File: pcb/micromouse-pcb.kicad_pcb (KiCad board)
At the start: 4 copper layers, 100 x 120 mm, 156 parts, among them J1 JST_PH_B2B-PH-K_1x02_P2.00mm_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, J5 JST_PH_B6B-PH-K_1x06_P2.00mm_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, J6 JST_PH_B6B-PH-K_1x06_P2.00mm_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, J7 USB_C_Receptacle_GCT_USB4105-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, J8 PinHeader_1x06_P2.54mm_Vertic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, Q1 SOT-23, Q16 SOT-23, Q17 SOT-23, Q18 SOT-23, Q19 SOT-23, Q2 LED_D5.0mm_IRBlack, Q20 SOT-23, Q21 SOT-23, Q22 SOT-23, Q23 SOT-23, Q24 SOT-23, Q25 SOT-23, Q26 SOT-23, Q27 SOT-23, Q28 SOT-23, Q29 SOT-23, Q3 LED_D5.0mm_IRBlack, Q30 SOT-23, Q31 SOT-23, Q32 SOT-23, Q33 SOT-23, Q4 LED_D5.0mm_IRBlack, Q5 LED_D5.0mm_IRBlack, Q6 LED_D5.0mm_IRBlack, Q7 LED_D5.0mm_IRBlack, SW1 SW_PUSH_6mm, SW2 SW_PUSH_6mm, SW3 SW_PUSH_6mm, SW4 SW_PUSH_6mm, SW5 SW_Slide_SPDT_Straight_CK_OS1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, U1 Texas_DRC0010J_ThermalVias, U2 SSOP-24_5.3x8.2mm_P0.65mm, U3 ESP32-S3-WROOM-1, U4 SOIC-24W_7.5x15.4mm_P1.27mm, U6 SOT-23-6

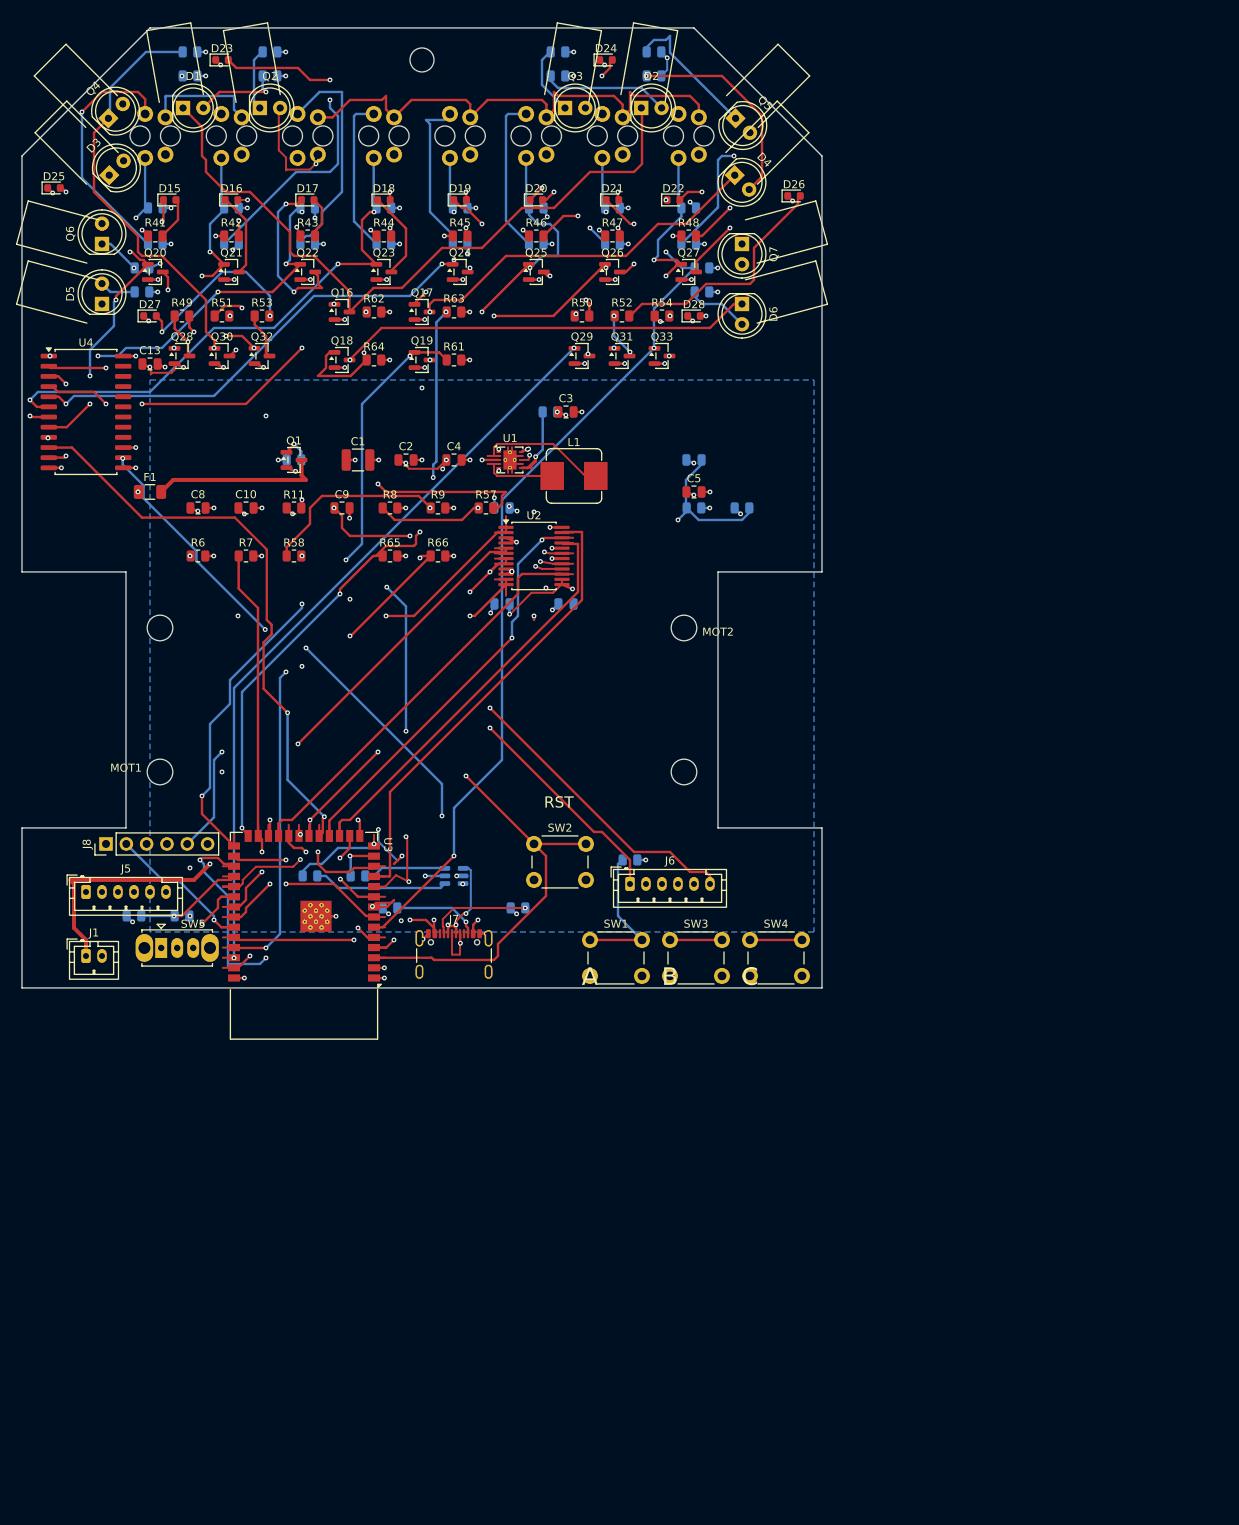
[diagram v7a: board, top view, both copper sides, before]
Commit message: Rev 6.1: 2S power, regulated 6V motors, BNO055 IMU, dual switches + full handoff
Design + firmware + verification COMPLETE and passing; PCB routed to 5
remaining unconnected edges (all in the USB-C connector fanout + the Q1 gate,
documented exactly in HANDOFF.md). This commit is a self-contained handoff so
the board can be finished on another machine with no human input.

Rev 6 (all 10 user requirements, each gated):
- 2S LiPo -> AP63203 3.3V + TPS54302 regulated 6.0V motor rail; DMP3098L
  reverse-FET (Vgs +/-20V, 2S-safe); dual switches (SW5 all / SW6 motors).
- BNO055 9-axis IMU on the centerline (I2C); external crystal DROPPED
  (internal oscillator, spec-supported) after it proved unroutable at the
  0.5mm-pitch LGA.
- Exact wall-sensor aims 0/45/90 deg with silk angle callouts; sensor
  outlines fully inside the board with a 3-5mm edge gap.
- Antenna spans a rear-edge U-notch (nothing outside the outline but shafts).
- USB-C direct D+/D-, IN/IN motor drive, per-cell battery monitoring.
- BOM entirely from Lion Circuits in-stock parts (turnkey, not LCSC).

circuit_tests 41/41 PASS (100% net + component coverage) and CAUGHT A REAL
BUG: the motor rail could never enable (R69 1M source impedance sagged the EN
divider below threshold) -- fixed R69->100k, R70->220k. ERC 0, netlist verify
PASS, 29 firmware pins gated, host sim ALL SCENARIOS PASS.

New tooling: finalize.py (silk->fab + RATSNEST-GATED copper cleanup),
sync_board_meta.py (board<->schematic parity metadata), gen_rev6_libs.py
(BNO055 + SRP4020TA footprints). Key lesson documented: kicad-cli's headless
"unconnected" is unreliable -- the pcbnew ratsnest is the connectivity truth,
and finalize refuses to strip unless it is already zero.

See HANDOFF.md for the exact remaining work, coordinates, gotchas (SWIG traps,
the connectivity trap), and the full finish + regenerate sequences.
Co-Authored-By: Claude Fable 5 <noreply@anthropic.com>
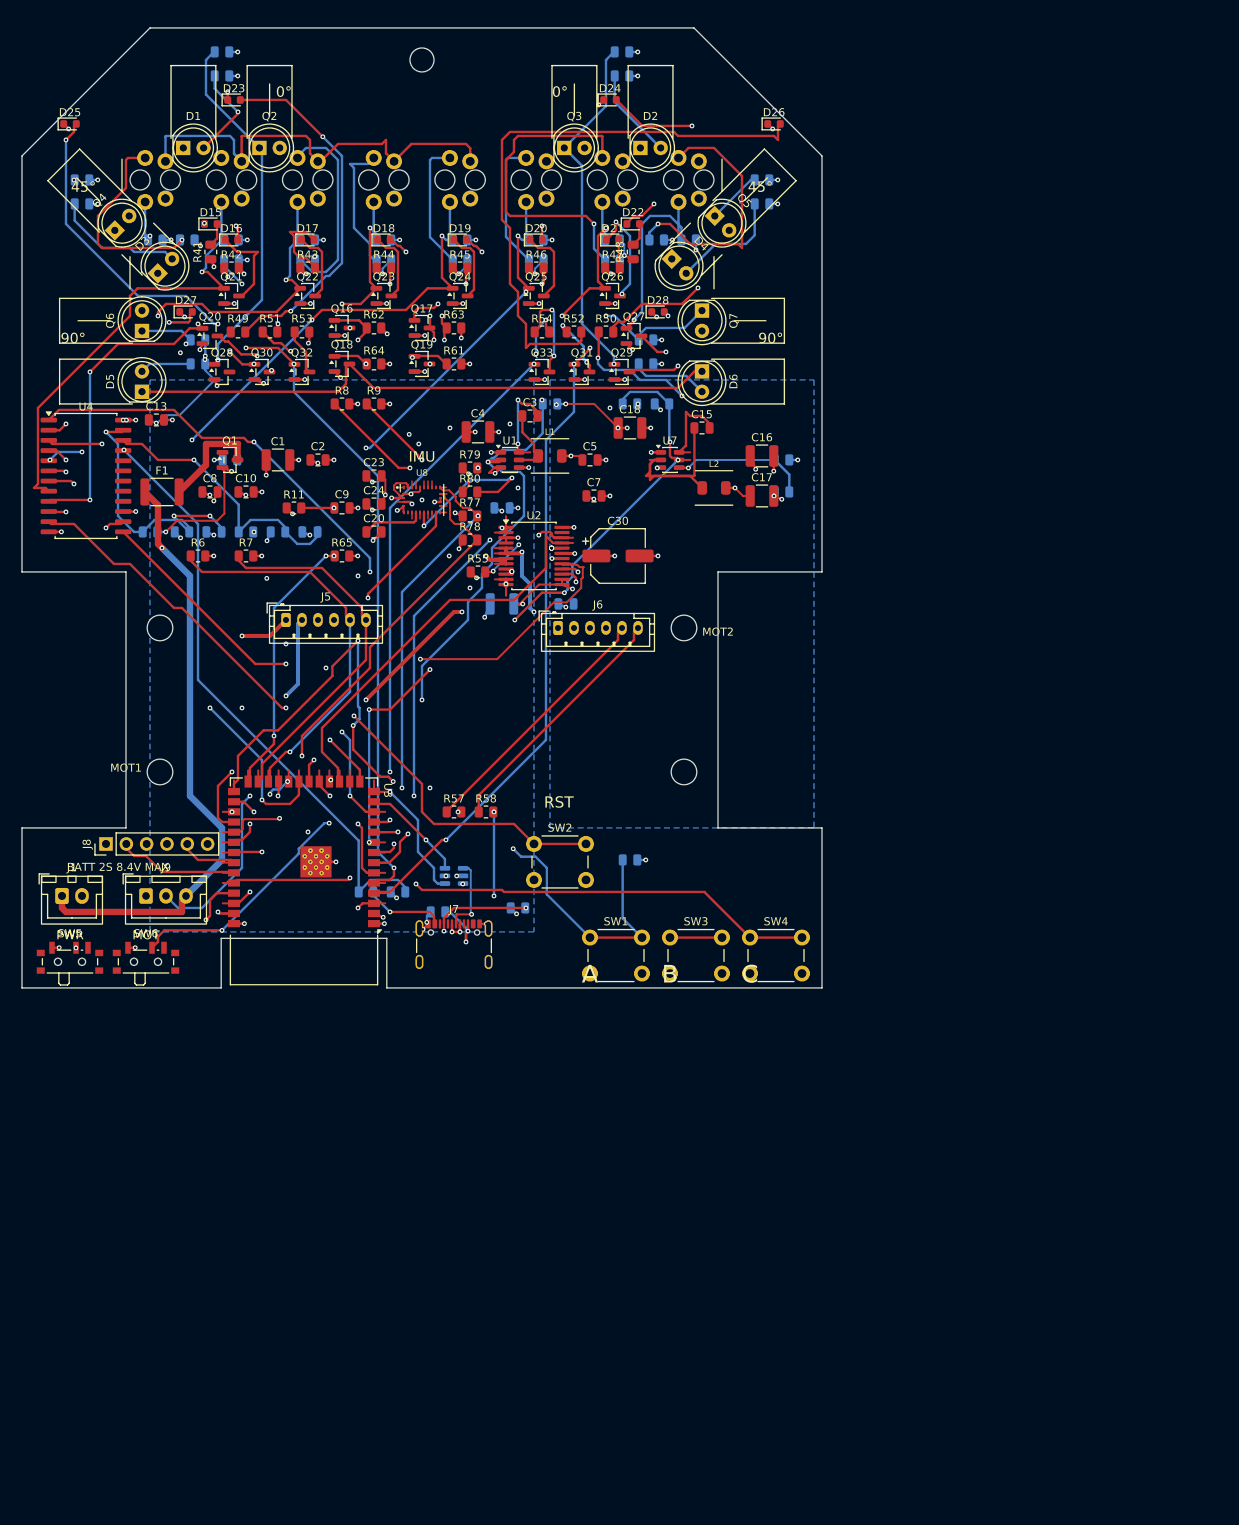
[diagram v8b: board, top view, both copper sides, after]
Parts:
- removed R59, R60, R66: R_0805_2012Metric, R_0805_2012Metric
- added C15: 100nF, C_0805_2012Metric, F.Cu at (85.0, 50.0)
- added C16: 22uF/25V, C_1210_3225Metric, F.Cu at (92.5, 53.5)
- added C17: 22uF/25V, C_1210_3225Metric, F.Cu at (92.5, 58.5)
- added C18: 10uF/25V, C_1210_3225Metric, F.Cu at (76.0, 50.0)
- added C19: C_0805_2012Metric, C_0805_2012Metric, B.Cu at (36.0, 63.0)
- added C20: C_0805_2012Metric, C_0805_2012Metric, F.Cu at (44.0, 63.0)
- added C23: C_0805_2012Metric, C_0805_2012Metric, F.Cu at (44.0, 56.0)
- added C24: 10uF, C_0805_2012Metric, F.Cu at (44.0, 59.5)
- added C30: 220uF/16V, CP_Elec_6.3x7.7, F.Cu at (74.5, 66.0)
- added C7: 22uF, C_0805_2012Metric, F.Cu at (71.5, 58.5)
- added J9: JST_XH_B3B-XH-A_1x03_P2.50mm_Vertical, JST_XH_B3B-XH-A_1x03_P2.50mm_Vertical, F.Cu at (15.5, 108.5)
- added L2: 4.7uH, L_Bourns_SRP4020TA, F.Cu at (86.5, 57.5)
- added R55: R_0805_2012Metric, R_0805_2012Metric, F.Cu at (57.0, 68.0)
- added R70: R_0805_2012Metric, R_0805_2012Metric, B.Cu at (76.0, 47.0)
- added R71: R_0805_2012Metric, R_0805_2012Metric, B.Cu at (80.0, 47.0)
- added R73: R_0805_2012Metric, R_0805_2012Metric, B.Cu at (95.0, 54.0)
- added R74: R_0805_2012Metric, R_0805_2012Metric, B.Cu at (95.0, 58.0)
- added R75: R_0805_2012Metric, R_0805_2012Metric, B.Cu at (28.0, 63.0)
- added R76: R_0805_2012Metric, R_0805_2012Metric, B.Cu at (32.0, 63.0)
- added R77: R_0805_2012Metric, R_0805_2012Metric, F.Cu at (56.0, 61.0)
- added R78: R_0805_2012Metric, R_0805_2012Metric, F.Cu at (56.0, 64.0)
- added R79: R_0805_2012Metric, R_0805_2012Metric, F.Cu at (56.0, 55.0)
- added R80: R_0805_2012Metric, R_0805_2012Metric, F.Cu at (56.0, 58.0)
- added SW6: SW_SPDT_PCM12, SW_SPDT_PCM12, F.Cu at (15.5, 116.4)
- added U7: SOT-23-6, SOT-23-6, F.Cu at (81.0, 54.0)
- added U8: VAL, BNO055, F.Cu at (50.0, 59.0)
- C1: value 100uF -> 10uF/25V
- C11, C4: value 10uF -> 10uF/25V; footprint C_0805_2012Metric -> C_1210_3225Metric
- F1: value Fuse_1206_3216Metric -> Fuse_1812_4532Metric; footprint Fuse_1206_3216Metric -> Fuse_1812_4532Metric
- J1: value JST_PH_B2B-PH-K_1x02_P2.00mm_Vertical -> JST_XH_B2B-XH-A_1x02_P2.50mm_Vertical; footprint JST_PH_B2B-PH-K_1x02_P2.00mm_Vertical -> JST_XH_B2B-XH-A_1x02_P2.50mm_Vertical
- L1: value 1.5uH -> 4.7uH; footprint L_Bourns_SRP7028A_7.3x6.6mm -> L_Bourns_SRP4020TA
- SW5: value SW_Slide_SPDT_Straight_CK_OS102011MS2Q -> SW_SPDT_PCM12; footprint SW_Slide_SPDT_Straight_CK_OS102011MS2Q -> SW_SPDT_PCM12
- U1: value Texas_DRC0010J_ThermalVias -> TSOT-23-6; footprint Texas_DRC0010J_ThermalVias -> TSOT-23-6
- moved R3 70.1 mm to (20.0, 63.0)
- moved R2 68.1 mm to (16.0, 63.0)
- moved C6 60.7 mm to (24.0, 63.0)
- moved J5 42.2 mm to (33.0, 74.0)
- moved R58 40.0 mm to (58.0, 98.0)
- moved R57 38.2 mm to (54.0, 98.0)
- moved J6 33.2 mm to (67.0, 75.0)
- moved R68 33.1 mm to (47.0, 108.0)
- moved R67 23.2 mm to (43.0, 108.0)
- moved R17 20.9 mm to (7.50, 19.0)
- moved R18 20.9 mm to (7.50, 22.0)
- moved R19 20.9 mm to (92.5, 19.0)
- moved R20 20.9 mm to (92.5, 22.0)
- moved R9 15.3 mm to (44.0, 47.0)
- moved Q33 15.1 mm to (65.0, 43.0)
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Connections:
- net Net-(J1-Pin_1) renamed BATT_RAW
- C11 pad 1: VM_BATT -> VM_6V
- C12 pad 1: VM_BATT -> VM_6V
- C3 pad 1: VM_BATT -> SW_3V3
- C3 pad 2: GND -> Net-(U1-BST)
- L1 pad 1: Net-(U1-L1) -> SW_3V3
- L1 pad 2: Net-(U1-L2) -> PLUS3V3
- U1 pad 2: Net-(U1-L2) -> PWR_EN
- U1 pad 3: GND -> VM_BATT
- U1 pad 4: Net-(U1-L1) -> GND
- U1 pad 5: VM_BATT -> SW_3V3
- U1 pad 6: PWR_EN -> Net-(U1-BST)
- U2 pad 13: VM_BATT -> VM_6V
- U2 pad 14: VM_BATT -> VM_6V
- U2 pad 15: PWMB -> PLUS3V3
- U2 pad 19: STBY -> Net-(U2-STBY)
- U2 pad 23: PWMA -> PLUS3V3
- U2 pad 24: VM_BATT -> VM_6V
- U3 pad 11: PWMA -> IMU_SDA
- U3 pad 12: VBAT_SENSE -> MUX_S3
- U3 pad 16: STBY -> unconnected-(U3-IO46-Pad16)
- U3 pad 23: PWMB -> IMU_SCL
- U3 pad 30: VBUS_SENSE -> IMU_INT
- U4 pad 13: GND -> MUX_S3
- U4 pad 21: unconnected-(U4-I10-Pad21) -> VBUS_SENSE
- U4 pad 22: unconnected-(U4-I9-Pad22) -> BAT_MID_SENSE
- U4 pad 23: unconnected-(U4-I8-Pad23) -> VBAT_SENSE
- U6 pad 4: Net-(R60-Pad1) -> USB_DP
- U6 pad 6: Net-(R59-Pad1) -> USB_DM
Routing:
- net MOT_EN: track 0.00 -> 111.2 mm, vias 0 -> 6
- net MOTB_N: track 113.0 -> 27.9 mm, vias 3 -> 2
- net MUX_S1: track 130.8 -> 51.6 mm, vias 3 -> 2
- net STBY: track 72.3 -> 0.00 mm, vias 4 -> 0
- net ENC2_A_S3: track 95.0 -> 34.4 mm
- net PWMA: track 60.3 -> 0.00 mm
- net VBUS_SENSE: track 15.2 -> 74.9 mm
- net VBAT_SENSE: track 91.0 -> 34.6 mm, vias 2 -> 3
- net IMU_INT: track 0.00 -> 55.1 mm, vias 0 -> 2
- net BAT_MID: track 0.00 -> 54.9 mm, vias 0 -> 2
- net IMU_SCL: track 0.00 -> 54.6 mm, vias 0 -> 2
- net PWMB: track 53.9 -> 0.00 mm
- net IMU_SDA: track 0.00 -> 53.4 mm, vias 0 -> 3
- net Net-(D22-K): track 16.8 -> 69.8 mm, vias 2 -> 3
- net MUX_S3: track 0.00 -> 52.2 mm, vias 0 -> 3
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- added copper zone on B.Cu, net VM_6V
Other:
- outline, holes or cut-outs redrawn
- board text added: "0°"
- board text added: "45°"
- board text added: "90°"
- board text added: "BATT 2S 8.4V MAX"
- board text added: "IMU"
- board text added: "MOT"
- board text added: "PWR"
